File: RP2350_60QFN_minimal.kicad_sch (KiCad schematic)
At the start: 43 parts, among them J1 USB_B_Micro, J2 Conn_02x18_Odd_Even, J3 Conn_02x18_Odd_Even, J4 SM03B-SRSS-TB, SW1 SW_Push, SW2 SW_Push, U1 RP2350_60QFN, U2 NCP1117-3.3_SOT223, U3 W25Q128JVS, Y1 ABM8-272-T3

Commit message: Decent core PCB setup, considering removing USB to make space for flash
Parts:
- removed U2: NCP1117-3.3_SOT223, Package_TO_SOT_SMD:SOT-223-3_TabPin2, symbol Regulator_Linear:NCP1117-3.3_SOT223
- added C21: 100n, Capacitor_SMD:C_1206_3216Metric, symbol Device:C
- added C6: 100n, Capacitor_SMD:C_0402_1005Metric, symbol Device:C
- added J1: Conn_01x02_Pin, Connector_AMASS:AMASS_XT30PW-M_1x02_P2.50mm_Horizontal, symbol Connector:Conn_01x02_Pin
- added J6: Bus Out, Connector_JST:JST_EH_S4B-EH_1x04_P2.50mm_Horizontal, symbol Connector:Conn_01x04_Socket
- added L1: 3.3u, RP2350_60QFN_minimal:L_pol_2016, symbol Device:L
- added R2: 1K, Resistor_SMD:R_0402_1005Metric, symbol Device:R
- added U2: LMR50410Y3FQDBVRQ1, footprints:DBV0006A-MFG, symbol LMR50410Y3FQDBVRQ1:LMR50410Y3FQDBVRQ1
- added U4: MAX3078E, Package_SO:SOIC-8_3.9x4.9mm_P1.27mm, symbol Interface_UART:MAX3078E
- C1: value 10u -> 2u2; footprint Capacitor_SMD:C_0805_2012Metric -> Capacitor_SMD:C_1206_3216Metric
- C10: renamed from C9; value 4.7u -> 4u7
- C11: renamed from C10; value 4.7u -> 4u7
- C20: renamed from C19; footprint Capacitor_SMD:C_0805_2012Metric -> Capacitor_SMD:C_0402_1005Metric
- C5: renamed from C6; value 4.7u -> 4u7
- C7: value 4.7u -> 4u7
- C8: renamed from C5; footprint Capacitor_SMD:C_0805_2012Metric -> Capacitor_SMD:C_0402_1005Metric
- J3: renamed from J2; footprint Connector_PinHeader_2.54mm:PinHeader_2x18_P2.54mm_Vertical -> Connector_PinHeader_2.54mm:PinHeader_1x18_P2.54mm_Vertical; symbol Connector_Generic:Conn_02x18_Odd_Even -> Connector:Conn_01x18_Socket
- J5: renamed from J3; footprint Connector_PinHeader_2.54mm:PinHeader_2x18_P2.54mm_Vertical -> Connector_PinHeader_2.54mm:PinHeader_1x18_P2.54mm_Vertical; symbol Connector_Generic:Conn_02x18_Odd_Even -> Connector:Conn_01x18_Socket
- L2: renamed from L1; value 3.3u -> 3u3
- R1, R9: value DNF -> 10K
- R10: value 0 -> 120R
- R3: renamed from R2; value 1k -> 1K
- R4, R6: value 1k -> 1K
- R5: value 33 -> 33R
- R7, R8: value 27 -> 27R
- U1: renamed from U3; footprint Package_SO:SOIC-8_5.23x5.23mm_P1.27mm -> Package_SO:SOIC-8_5.3x5.3mm_P1.27mm
- renumbered C11 to C12, C12 to C13, C13 to C14, C14 to C15, C15 to C16, C16 to C17, C17 to C18, C18 to C19, C3 to C2, C4 to C3, C2 to C4, C8 to C9, J1 to J2, U1 to U3
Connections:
- net +3V3: now also J3.1 (Pin_1), L1.2, U2.3 (FB), U4.8 (VCC); no longer J3.2 (Pin_2), R1.1
- net FLASH_SS: now also R6.1, U3.60 (QSPI_SS); no longer R1.2, R10.2, R9.2
- net GND: now also J3.18 (Pin_18), R9.2, C21.2, J1.2 (Pin_2), J6.1 (Pin_1), R2.2, U2.2 (GND), U4.5 (GND); no longer J3.1 (Pin_1), J3.11 (Pin_11), J3.13 (Pin_13), J3.15 (Pin_15), J3.17 (Pin_17), J3.19 (Pin_19), J3.21 (Pin_21), J3.23 (Pin_23), J3.25 (Pin_25), J3.27 (Pin_27), J3.29 (Pin_29), J3.3 (Pin_3), J3.31 (Pin_31), J3.33 (Pin_33), J3.35 (Pin_35), J3.36 (Pin_36), J3.5 (Pin_5), J3.7 (Pin_7), J3.9 (Pin_9), J5.10 (Pin_10), J5.12 (Pin_12), J5.14 (Pin_14), J5.16 (Pin_16), J5.2 (Pin_2), J5.20 (Pin_20), J5.22 (Pin_22), J5.24 (Pin_24), J5.26 (Pin_26), J5.28 (Pin_28), J5.30 (Pin_30), J5.32 (Pin_32), J5.34 (Pin_34), J5.35 (Pin_35), J5.36 (Pin_36), J5.4 (Pin_4), J5.6 (Pin_6), J5.8 (Pin_8)
- net GPIO0: now also J3.2 (Pin_2); no longer J3.4 (Pin_4), R9.1
- net GPIO1: now also J3.3 (Pin_3); no longer J3.6 (Pin_6)
- net GPIO10: now also J3.12 (Pin_12); no longer J3.24 (Pin_24)
- net GPIO11: now also J3.13 (Pin_13); no longer J3.26 (Pin_26)
- net GPIO12: now also J3.14 (Pin_14); no longer J3.28 (Pin_28)
- net GPIO13: now also J3.15 (Pin_15); no longer J3.30 (Pin_30)
- net GPIO14: now also J3.16 (Pin_16); no longer J3.32 (Pin_32)
- net GPIO15: now also J3.17 (Pin_17); no longer J3.34 (Pin_34)
- net GPIO16: now also J5.14 (Pin_14); no longer J5.27 (Pin_27)
- net GPIO17: now also J5.13 (Pin_13); no longer J5.25 (Pin_25)
- net GPIO18: now also J5.12 (Pin_12); no longer J5.23 (Pin_23)
- net GPIO19: now also J5.11 (Pin_11); no longer J5.21 (Pin_21)
- net GPIO2: now also J3.4 (Pin_4); no longer J3.8 (Pin_8)
- net GPIO20: now also J5.10 (Pin_10); no longer J5.19 (Pin_19)
- net GPIO21: now also J5.9 (Pin_9); no longer J5.17 (Pin_17)
- net GPIO22: now also J5.8 (Pin_8); no longer J5.15 (Pin_15)
- net GPIO23: now also J5.7 (Pin_7); no longer J5.13 (Pin_13)
- net GPIO24: now also J5.6 (Pin_6); no longer J5.11 (Pin_11)
- net GPIO25: now also J5.5 (Pin_5); no longer J5.9 (Pin_9)
- net GPIO26_ADC0: now also J5.4 (Pin_4); no longer J5.7 (Pin_7)
- net GPIO27_ADC1: now also J5.3 (Pin_3); no longer J5.5 (Pin_5)
- net GPIO28_ADC2: now also J5.2 (Pin_2); no longer J5.3 (Pin_3)
- net GPIO29_ADC3: now also R1.2, R2.1
- net GPIO3: now also J3.5 (Pin_5); no longer J3.10 (Pin_10)
- net GPIO4: now also J3.6 (Pin_6); no longer J3.12 (Pin_12)
- net GPIO5: now also J3.7 (Pin_7); no longer J3.14 (Pin_14)
- net GPIO6: now also J3.8 (Pin_8); no longer J3.16 (Pin_16)
- net GPIO7: now also J3.9 (Pin_9), R9.1, U4.2 (~{RE}), U4.3 (DE); no longer J3.18 (Pin_18)
- net GPIO8: now also J3.10 (Pin_10), U4.4 (DI); no longer J3.20 (Pin_20)
- net GPIO9: now also J3.11 (Pin_11), U4.1 (RO); no longer J3.22 (Pin_22)
- net RUN: now also J5.15 (Pin_15); no longer J5.29 (Pin_29)
- net SWCLK: now also J5.17 (Pin_17); no longer J5.33 (Pin_33)
- net SWD: now also J5.16 (Pin_16); no longer J5.31 (Pin_31)
- removed net QSPI_SS: R10.1, R6.1, U3.60 (QSPI_SS)
- net VBUS: no longer names the net of J2.1 (VBUS)
- net VBUS: no longer C1.1
- new net: C6.1, L1.1, U2.6 (SW)
- new net: C6.2, U2.1 (CB)
- new net +24V: C1.1, C21.1, J1.1 (Pin_1), J6.2 (Pin_2), R1.1, U2.4 (EN), U2.5 (VIN)
- new net RS485-A: J6.3 (Pin_3), R10.2, U4.6 (A)
- new net RS485-B: J6.4 (Pin_4), R10.1, U4.7 (B)
- no-connect marks 1 -> 2
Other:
- moved on the sheet: C1, C20, C8, J2, J4

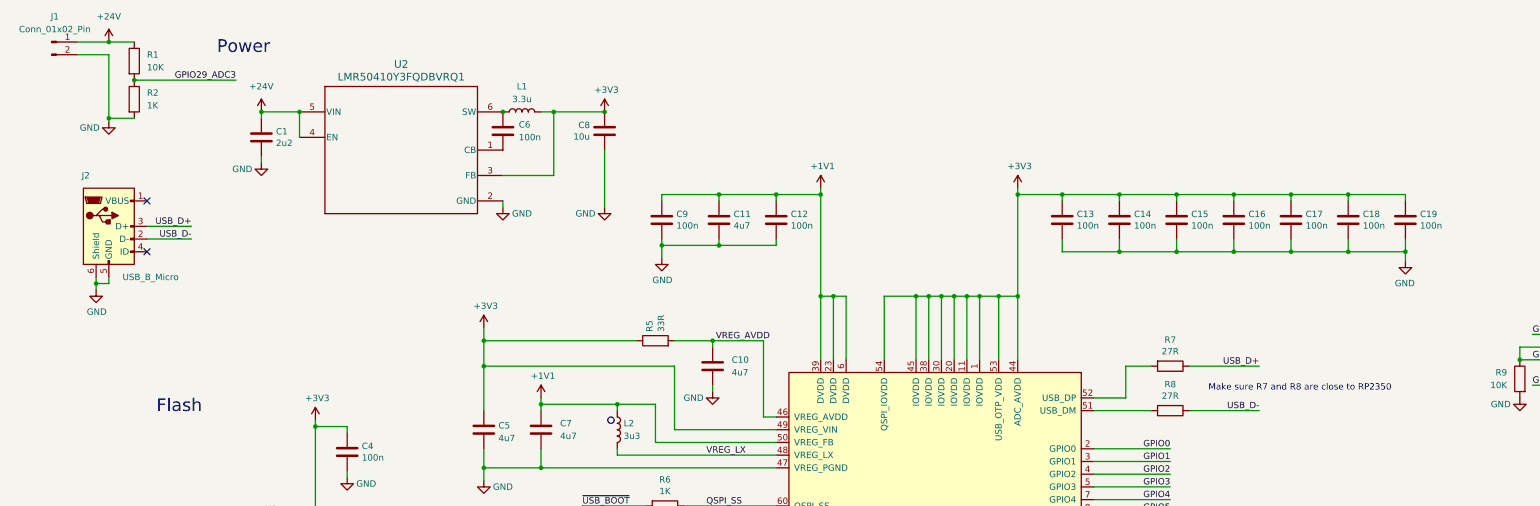
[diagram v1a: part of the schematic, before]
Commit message: fucking reversed polarity on the XT30
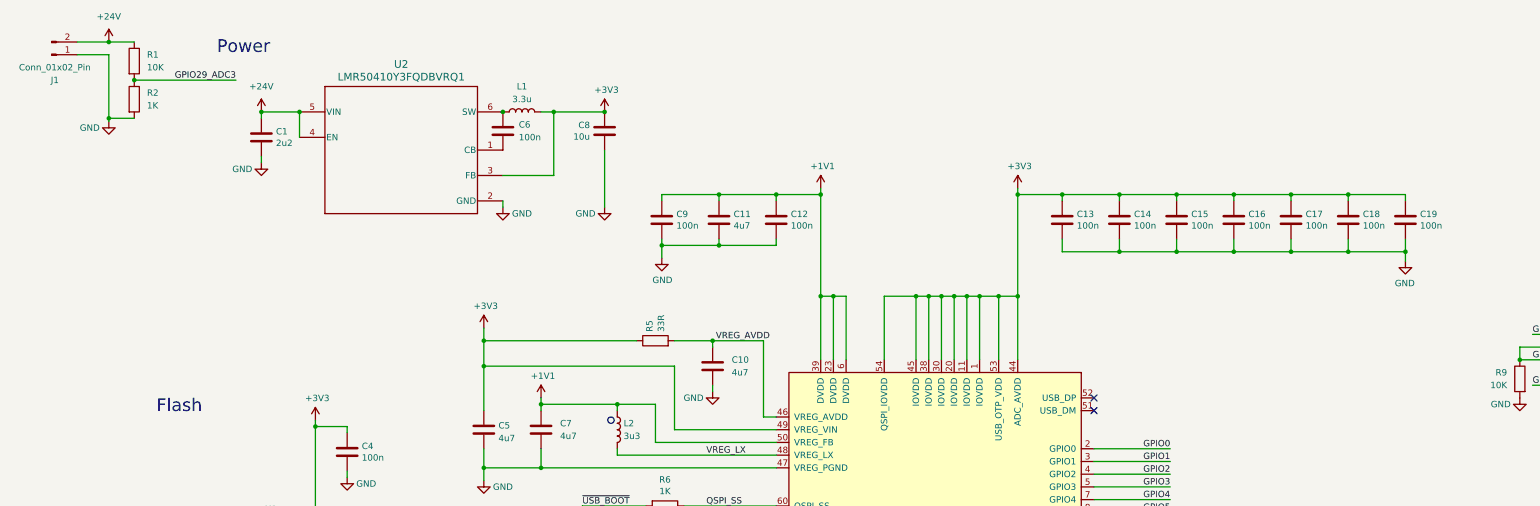
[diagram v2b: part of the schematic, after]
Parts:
- removed J2: USB_B_Micro, Connector_USB:USB_Micro-B_Amphenol_10103594-0001LF_Horizontal, symbol Connector:USB_B_Micro
- removed R7, R8: 27R, Resistor_SMD:R_0402_1005Metric, symbol Device:R
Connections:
- net +24V: now also J1.2 (Pin_2); no longer J1.1 (Pin_1)
- net GND: now also J1.1 (Pin_1); no longer J1.2 (Pin_2)
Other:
- note removed: "Make sure R7 and R8 are close to RP2350"

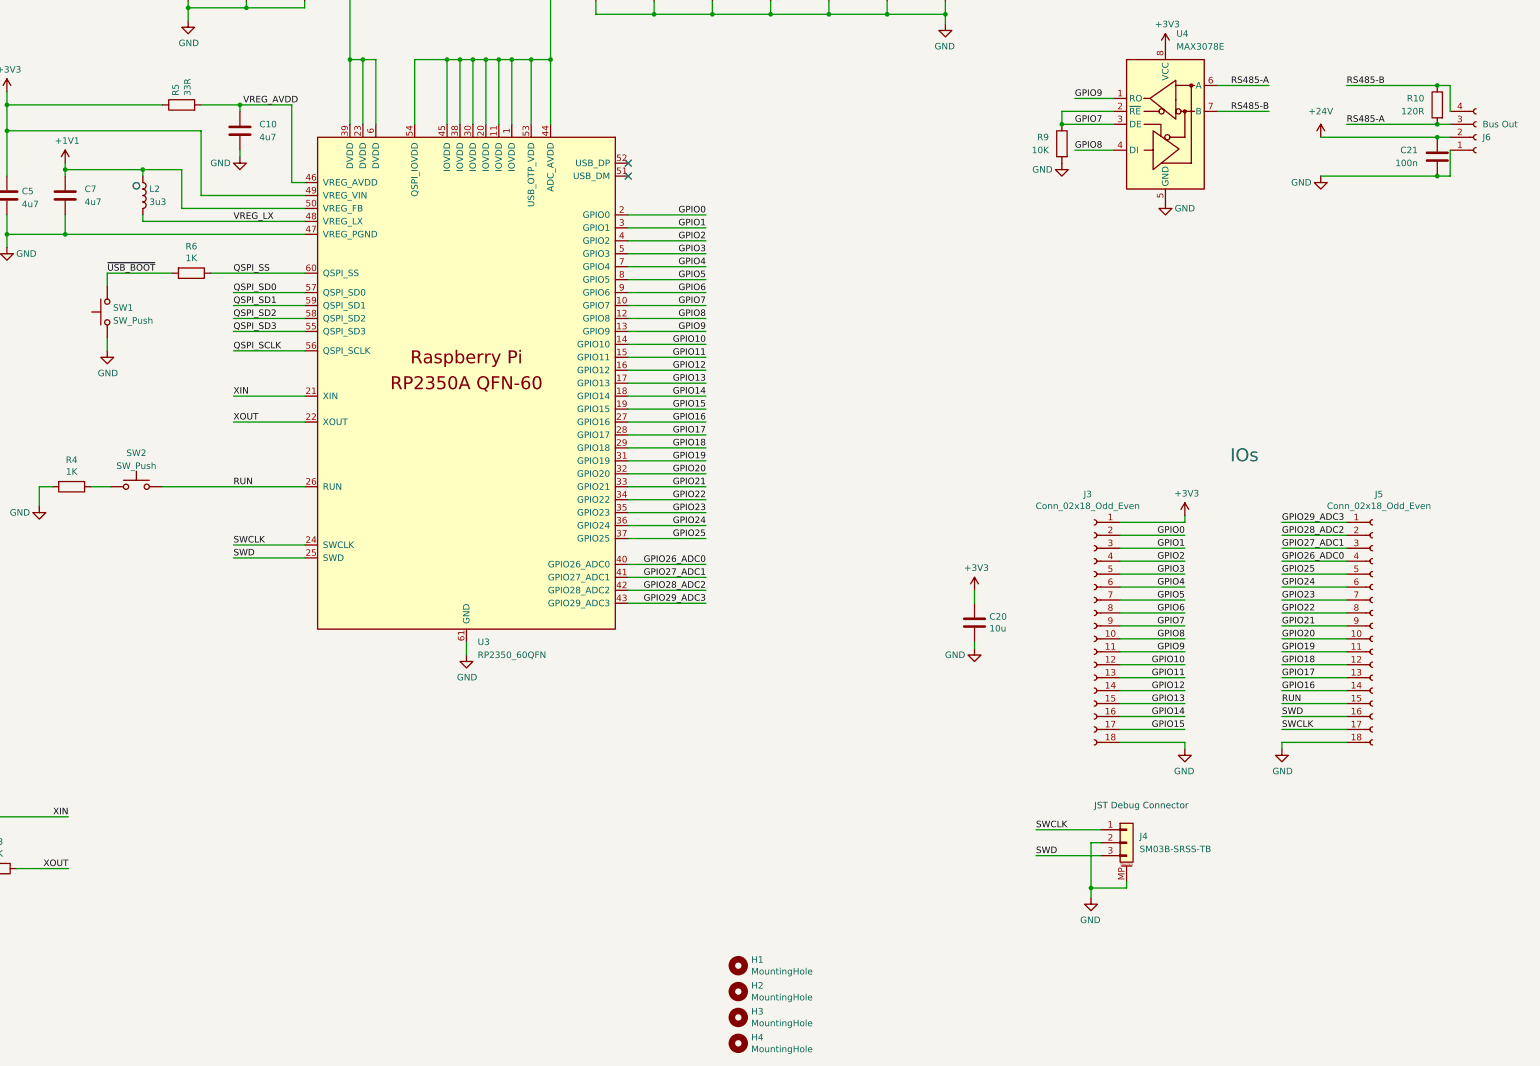
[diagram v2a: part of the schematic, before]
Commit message: Finished design without wifi & unchecked
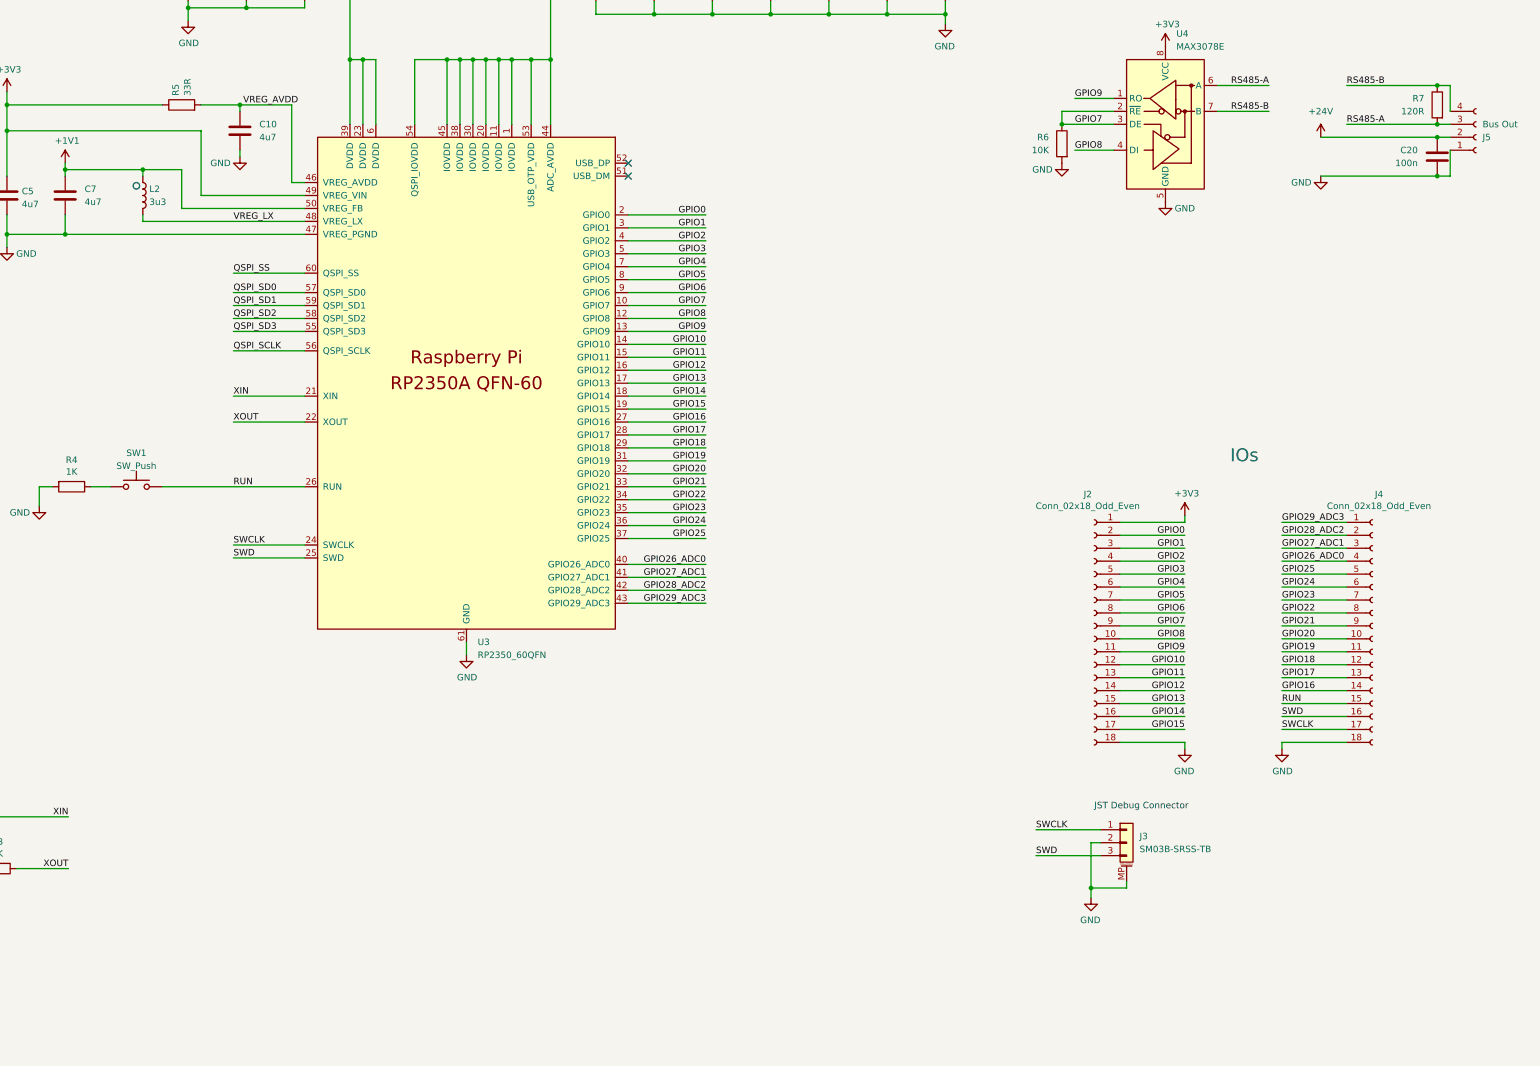
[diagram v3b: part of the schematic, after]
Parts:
- removed C20: 10u, Capacitor_SMD:C_0402_1005Metric, symbol Device:C
- removed H1, H2, H3, H4: MountingHole, MountingHole:MountingHole_2.7mm_M2.5, symbol Mechanical:MountingHole
- removed R6: 1K, Resistor_SMD:R_0402_1005Metric, symbol Device:R
- removed SW1: SW_Push, Button_Switch_SMD:SW_Push_1P1T_NO_Vertical_Wuerth_434133025816, symbol Switch:SW_Push
- C10, C11, C15, C17, C18: footprint Capacitor_SMD:C_0402_1005Metric -> RP2350_60QFN_minimal:C_0402_1005Metric_small_pads
- C20: renamed from C21; footprint Capacitor_SMD:C_1206_3216Metric -> Capacitor_SMD:C_0402_1005Metric
- renumbered J3 to J2, J4 to J3, J5 to J4, J6 to J5, R9 to R6, R10 to R7, SW2 to SW1

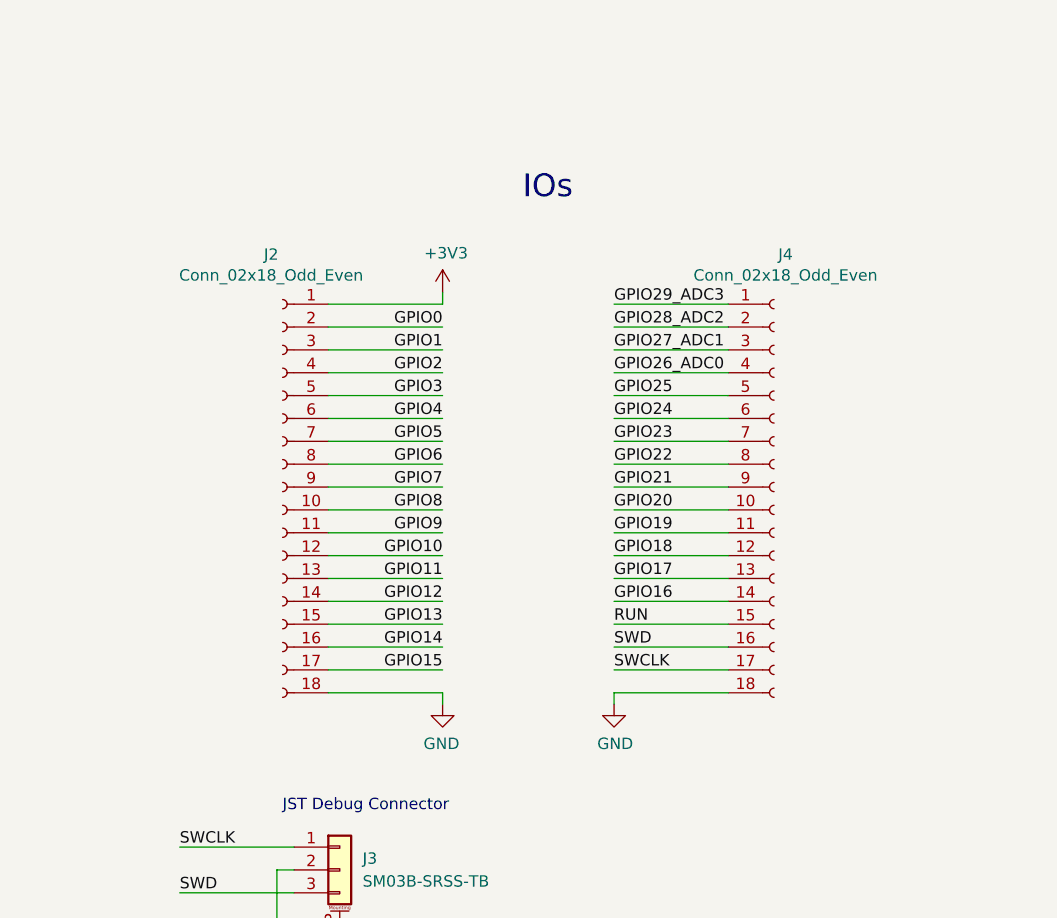
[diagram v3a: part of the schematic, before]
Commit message: Find parts on LCSC
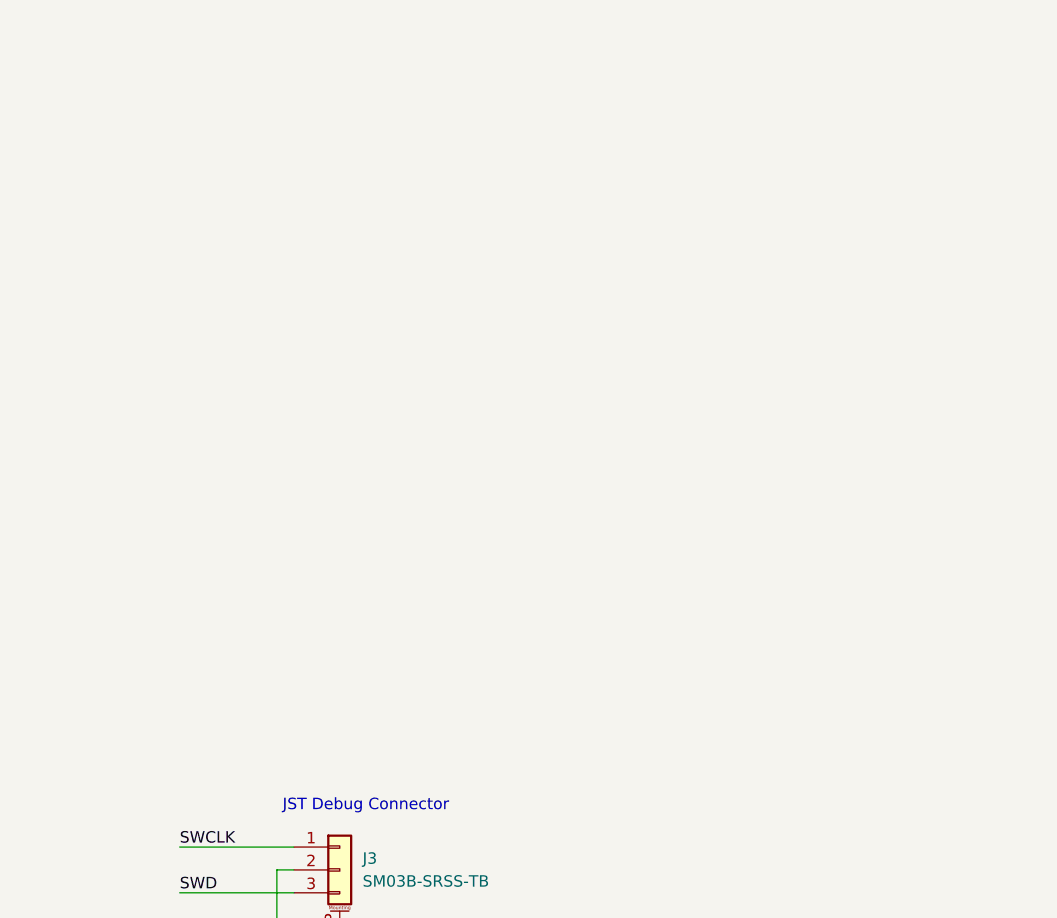
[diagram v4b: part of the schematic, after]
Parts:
- removed J2, J4: Conn_02x18_Odd_Even, Connector_PinHeader_2.54mm:PinHeader_1x18_P2.54mm_Vertical, symbol Connector:Conn_01x18_Socket
- C1, C12, C13, C14, C15, C16, C17, C18, C19, C20, C4, C6, C9: LCSC PN (none) -> C307419
- C10, C11, C5, C7: LCSC PN (none) -> C2932473
- C2, C3: LCSC PN (none) -> C326803
- C8: LCSC PN (none) -> C76991
- J1: LCSC PN (none) -> C431092
- J3: LCSC PN (none) -> C160403
- J5: LCSC PN (none) -> C265068
- L1, L2: LCSC PN (none) -> C42411119
- R1: LCSC PN (none) -> C190095
- R2: LCSC PN (none) -> C852624
- R3, R4: LCSC PN (none) -> C106235
- R5: LCSC PN (none) -> C138002
- R6: LCSC PN (none) -> C60490
- R7: LCSC PN (none) -> C114758
- SW1: LCSC PN (none) -> C18198078
- U1: LCSC PN (none) -> C113767
- U2: LCSC PN (none) -> C5219374
- U3: LCSC PN (none) -> C42411118
- U4: LCSC PN (none) -> C42396723
- Y1: LCSC PN (none) -> C20625731
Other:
- note removed: "IOs"
